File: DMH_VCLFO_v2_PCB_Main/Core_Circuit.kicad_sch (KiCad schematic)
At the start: 21 parts, among them Q5 BS170, U10 TL074, U11 TL074

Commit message: Designed osc core based on slew module
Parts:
- removed C7: 10nF, Capacitor_THT:C_Disc_D4.3mm_W1.9mm_P5.00mm, symbol Device:C
- removed Q5: BS170, Package_TO_SOT_THT:TO-92_Inline, symbol Transistor_FET:BS170
- removed R48, R49: 51k, Resistor_THT:R_Axial_DIN0207_L6.3mm_D2.5mm_P7.62mm_Horizontal, symbol Device:R_US
- removed U10, U11: TL074, Package_DIP:DIP-14_W7.62mm_Socket, symbol Amplifier_Operational:TL074
- added C13, C14, C15: 100nF, Capacitor_THT:C_Disc_D4.3mm_W1.9mm_P5.00mm, symbol Device:C
- added C14: 22nF, Capacitor_THT:C_Disc_D4.3mm_W1.9mm_P5.00mm, symbol Device:C
- added C15: 220nF, Capacitor_THT:C_Disc_D4.3mm_W1.9mm_P5.00mm, symbol Device:C
- added C7: 2.2nF, Capacitor_THT:C_Disc_D4.3mm_W1.9mm_P5.00mm, symbol Device:C
- added C7: 10pF, Capacitor_THT:C_Disc_D3.0mm_W2.0mm_P2.50mm, symbol Device:C
- added J12: Conn_02x06_Top_Bottom, Connector_PinHeader_2.54mm:PinHeader_2x06_P2.54mm_Horizontal, symbol Connector_Generic:Conn_02x06_Top_Bottom
- added J13 (x2): Conn_02x03_Top_Bottom, Connector_PinHeader_2.54mm:PinHeader_2x03_P2.54mm_Horizontal, symbol Connector_Generic:Conn_02x03_Top_Bottom
- added J14, J16: Conn_02x03_Top_Bottom, Connector_PinSocket_2.54mm:PinSocket_2x03_P2.54mm_Vertical, symbol Connector_Generic:Conn_02x03_Top_Bottom
- added J15: Conn_02x06_Top_Bottom, Connector_PinSocket_2.54mm:PinSocket_2x06_P2.54mm_Vertical, symbol Connector_Generic:Conn_02x06_Top_Bottom
- added Q10, Q9: BC558, Package_TO_SOT_THT:TO-92L_Inline_Wide, symbol Transistor_BJT:BC558
- added Q5, Q8: BC548, Package_TO_SOT_THT:TO-92L_Inline_Wide, symbol Transistor_BJT:BC548
- added R87, R99: 100k, Resistor_THT:R_Axial_DIN0207_L6.3mm_D2.5mm_P7.62mm_Horizontal, symbol Device:R_US
- added R88: 220k, Resistor_THT:R_Axial_DIN0207_L6.3mm_D2.5mm_P7.62mm_Horizontal, symbol Device:R_US
- added R93: 1k, Resistor_THT:R_Axial_DIN0207_L6.3mm_D2.5mm_P7.62mm_Horizontal, symbol Device:R_US
- added U5, U6: TL074, Package_DIP:DIP-14_W7.62mm_Socket, symbol Amplifier_Operational:TL074
- C6: value 1uF -> 10pF; footprint Capacitor_THT:C_Disc_D4.3mm_W1.9mm_P5.00mm -> Capacitor_THT:C_Disc_D3.0mm_W2.0mm_P2.50mm
- R40: value 100k -> 1k; now not fitted
- R45: value 100k -> 82k
- R46: value 51k -> 100k
- R52: value 3k9 -> 220k
- R56: value 10k -> 100k
- R59: value 10k -> 1k8
- R72, R73: value 100k -> 1k8
- R84: value 680k -> 1k8
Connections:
- net Pot In is gone; now on an unnamed net: R38.1
- net Rng_Sw_2 is gone; now on an unnamed net: R45.2
- net GND: now also C12.2, R43.2, R59.1, R72.1, R73.2, C13.1, C14.2, C15.1, J12.5 (Pin_5), J12.6 (Pin_6), J13.5 (Pin_5), J13.6 (Pin_6), J14.5 (Pin_5), J14.6 (Pin_6), J15.5 (Pin_5), J15.6 (Pin_6), U5.3 (+), U6.12 (+), U6.5 (+); no longer R40.1, R52.2, R56.2, R73.1
- net at R53.1: now also Q10.3 (E), Q5.3 (E), Q8.3 (E), Q9.3 (E); no longer R52.1
- net at R56.1: now also R38.2, R87.1, U5.1; no longer R59.1
- net at R43.1: now also U6.10 (+); no longer R40.2
- net A_Sqr_S: now reaches R46.2
- net A_Sqr_S: now also R45.1, C7.2, J13.3 (Pin_3), U6.8
- net at R72.2: now also Q8.2 (B); no longer R73.2
- net CV In: no longer names the net of R37.1
- net CV In: now also R99.1, U5.2 (-)
- net Rng_Sw_1: no longer names the net of C6.1
- net Rng_Sw_1: now also R46.1, Q10.1 (C), Q5.1 (C), U6.13 (-)
- net Rng_Sw_3 renamed +12V
- net +12V: now also R52.1, C14.1, J13.1 (Pin_1), J14.1 (Pin_1), R88.1, U5.4 (V+), U6.4 (V+)
- removed net Sqr_Raw: R53.2, R59.2, R72.1
- net Tri_Raw: no longer names the net of C6.2
- net Tri_Raw: now also R53.2, U6.14; no longer C12.2
- new net: Q10.2 (B), R84.1
- new net: C7.1, R40.1, U6.9 (-)
- new net: C14.1, C15.1, C7.1, Q8.1 (C), Q9.1 (C), U6.6 (-)
- new net: Q5.2 (B), R52.2, R56.2, R59.2
- new net: Q9.2 (B), R73.1, R87.2, R88.2
- new net: R93.2, U6.7
- new net -12V: C13.2, C15.2, J13.3 (Pin_3), J13.4 (Pin_4), J14.3 (Pin_3), J14.4 (Pin_4), U5.11 (V-), U6.11 (V-)
- new net A_CV_M: J16.5 (Pin_5)
- new net A_CV_S: J13.5 (Pin_5), R37.2
- new net A_Freq_Pot_p2_M: R99.2
- new net A_Rng_Sw_p1_M: J15.12 (Pin_12)
- new net A_Rng_Sw_p1_S: C14.2, J12.12 (Pin_12)
- new net A_Rng_Sw_p3_M: J15.11 (Pin_11)
- new net A_Rng_Sw_p3_S: C15.2, J12.11 (Pin_11)
- new net A_Sqr_M: J16.3 (Pin_3)
- new net A_Tri_M: J16.6 (Pin_6)
- new net A_Tri_S: C7.2, J13.6 (Pin_6), R40.2, R93.1
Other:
- note added: "22pF in bb"
- note added: "Check if this 1k can be removed"
- note added: "Check if this is really the square output"

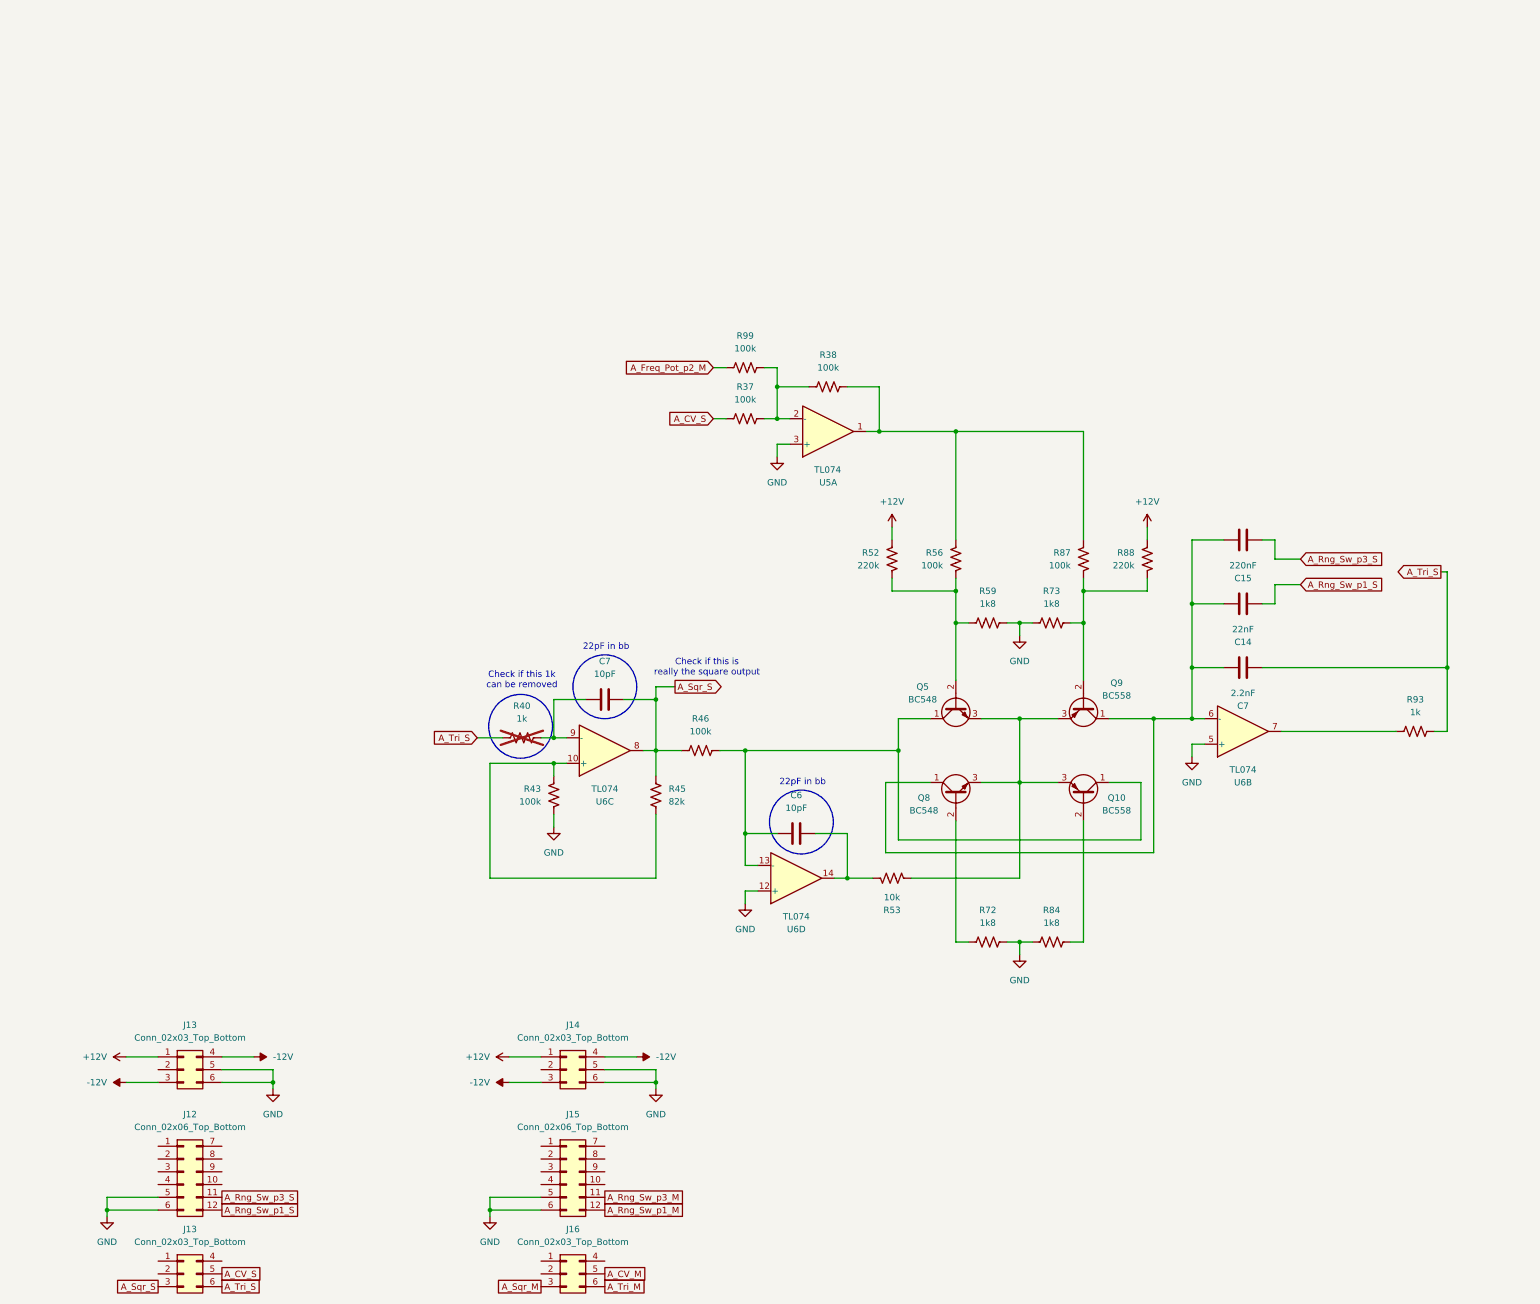
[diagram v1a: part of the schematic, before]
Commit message: Adapted sync reset circuit
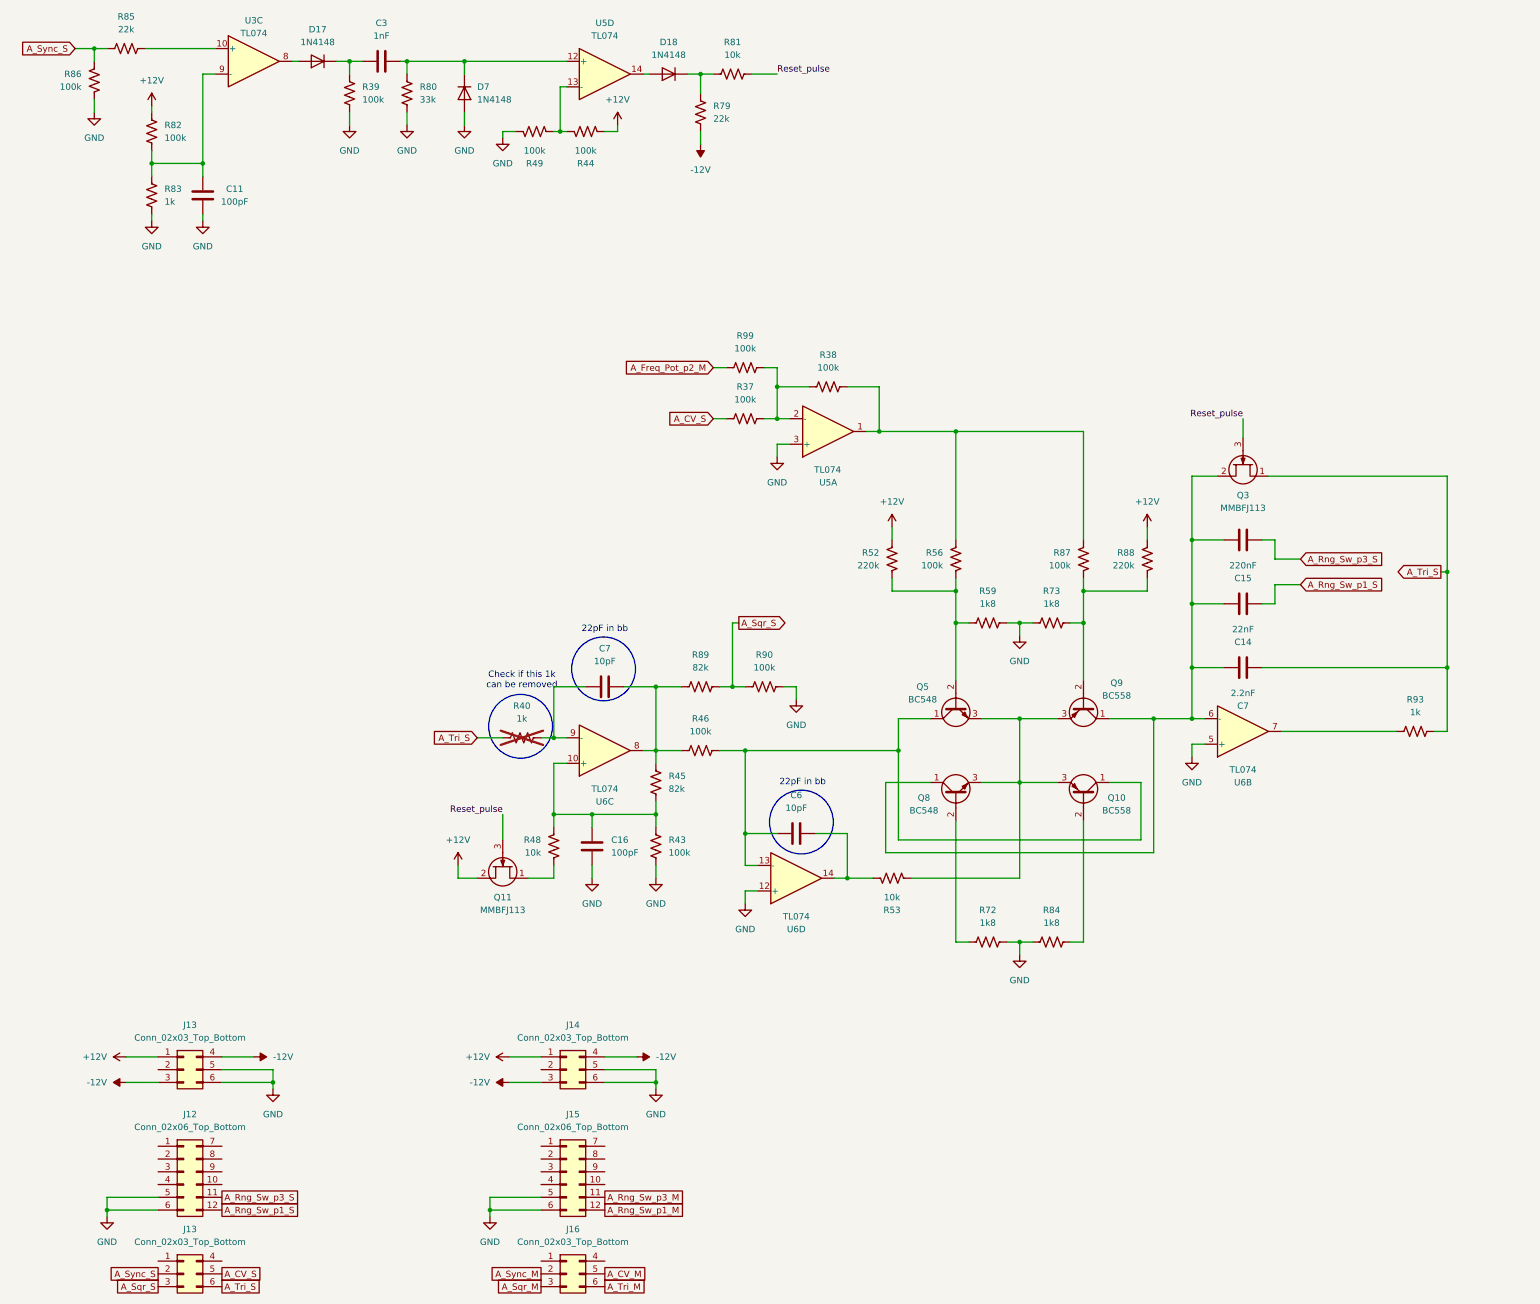
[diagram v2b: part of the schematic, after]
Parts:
- added C11: 100pF, Capacitor_THT:C_Disc_D4.3mm_W1.9mm_P5.00mm, symbol Device:C
- added C16: 100pF, Capacitor_THT:C_Disc_D3.0mm_W2.0mm_P2.50mm, symbol Device:C
- added C3: 1nF, Capacitor_THT:C_Disc_D4.3mm_W1.9mm_P5.00mm, symbol Device:C
- added D17, D18, D7: 1N4148, Diode_THT:D_DO-35_SOD27_P7.62mm_Horizontal, symbol Diode:1N4148
- added Q11, Q3: MMBFJ113, Package_TO_SOT_SMD:SOT-23, symbol Transistor_FET:MMBFJ113
- added R39, R44, R49, R82, R86, R90: 100k, Resistor_THT:R_Axial_DIN0207_L6.3mm_D2.5mm_P7.62mm_Horizontal, symbol Device:R_US
- added R48, R81: 10k, Resistor_THT:R_Axial_DIN0207_L6.3mm_D2.5mm_P7.62mm_Horizontal, symbol Device:R_US
- added R79, R85: 22k, Resistor_THT:R_Axial_DIN0207_L6.3mm_D2.5mm_P7.62mm_Horizontal, symbol Device:R_US
- added R80: 33k, Resistor_THT:R_Axial_DIN0207_L6.3mm_D2.5mm_P7.62mm_Horizontal, symbol Device:R_US
- added R83: 1k, Resistor_THT:R_Axial_DIN0207_L6.3mm_D2.5mm_P7.62mm_Horizontal, symbol Device:R_US
- added R89: 82k, Resistor_THT:R_Axial_DIN0207_L6.3mm_D2.5mm_P7.62mm_Horizontal, symbol Device:R_US
- added U3: TL074, Package_DIP:DIP-14_W7.62mm_Socket, symbol Amplifier_Operational:TL074
- added unit 4 of U5
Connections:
- net +12V: now also Q11.2 (S), R44.1, R82.1
- net -12V: now also R79.2
- net A_Sqr_S: now also R89.1, R90.2; no longer C7.2, R45.1, R46.2, U6.8
- net A_Tri_S: now also Q3.1 (D)
- net GND: now also C11.1, C16.1, D7.2 (A), R39.2, R49.2, R80.2, R83.2, R86.1, R90.1
- net at R43.1, R45.2, U6.10 (+): now also C16.2, R48.1
- net at C14.1, C15.1, C7.1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: now also Q3.2 (S)
- net A_Sync_M: now reaches J16.2 (Pin_2)
- net A_Sync_S: now reaches J13.2 (Pin_2)
- net A_Sync_S: now also R85.1, R86.2
- new net: C3.1, D17.1 (K), R39.1
- new net: C7.2, R45.1, R46.2, R89.2, U6.8
- new net: R85.2, U3.10 (+)
- new net: C11.2, R82.2, R83.1, U3.9 (-)
- new net: R44.2, R49.1, U5.13 (-)
- new net: Q11.1 (D), R48.2
- new net: D18.1 (K), R79.1, R81.2
- new net: C3.2, D7.1 (K), R80.1, U5.12 (+)
- new net: D17.2 (A), U3.8
- new net: D18.2 (A), U5.14
- new net Reset_pulse: Q11.3 (G), Q3.3 (G), R81.1
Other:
- note removed: "Check if this is really the square output"
- moved on the sheet: C7, R43, R45

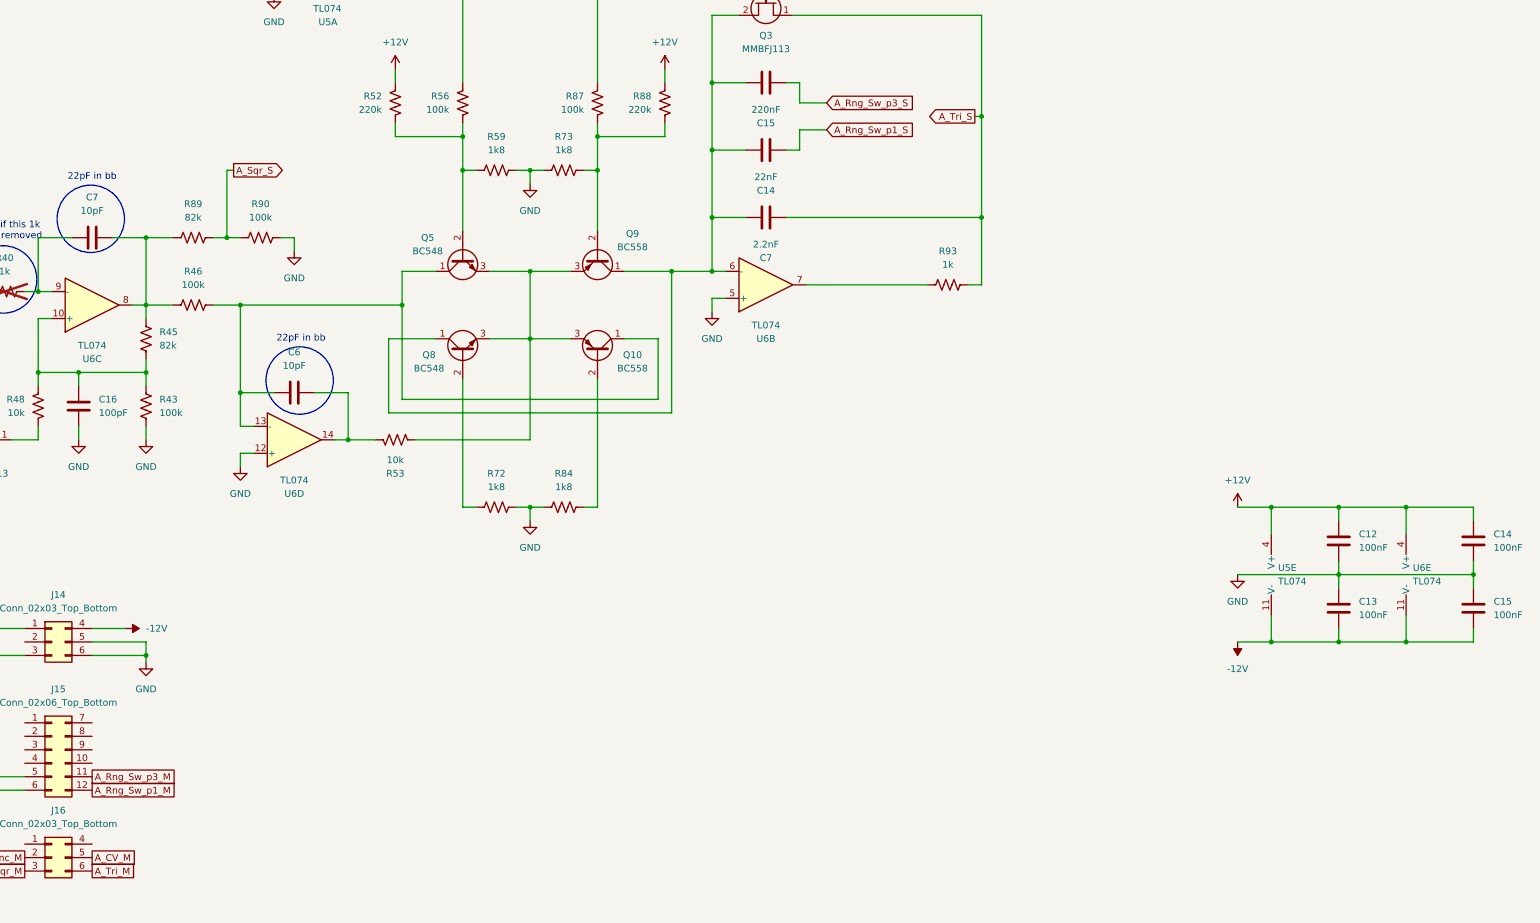
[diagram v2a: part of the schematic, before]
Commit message: Adapted saw shaper
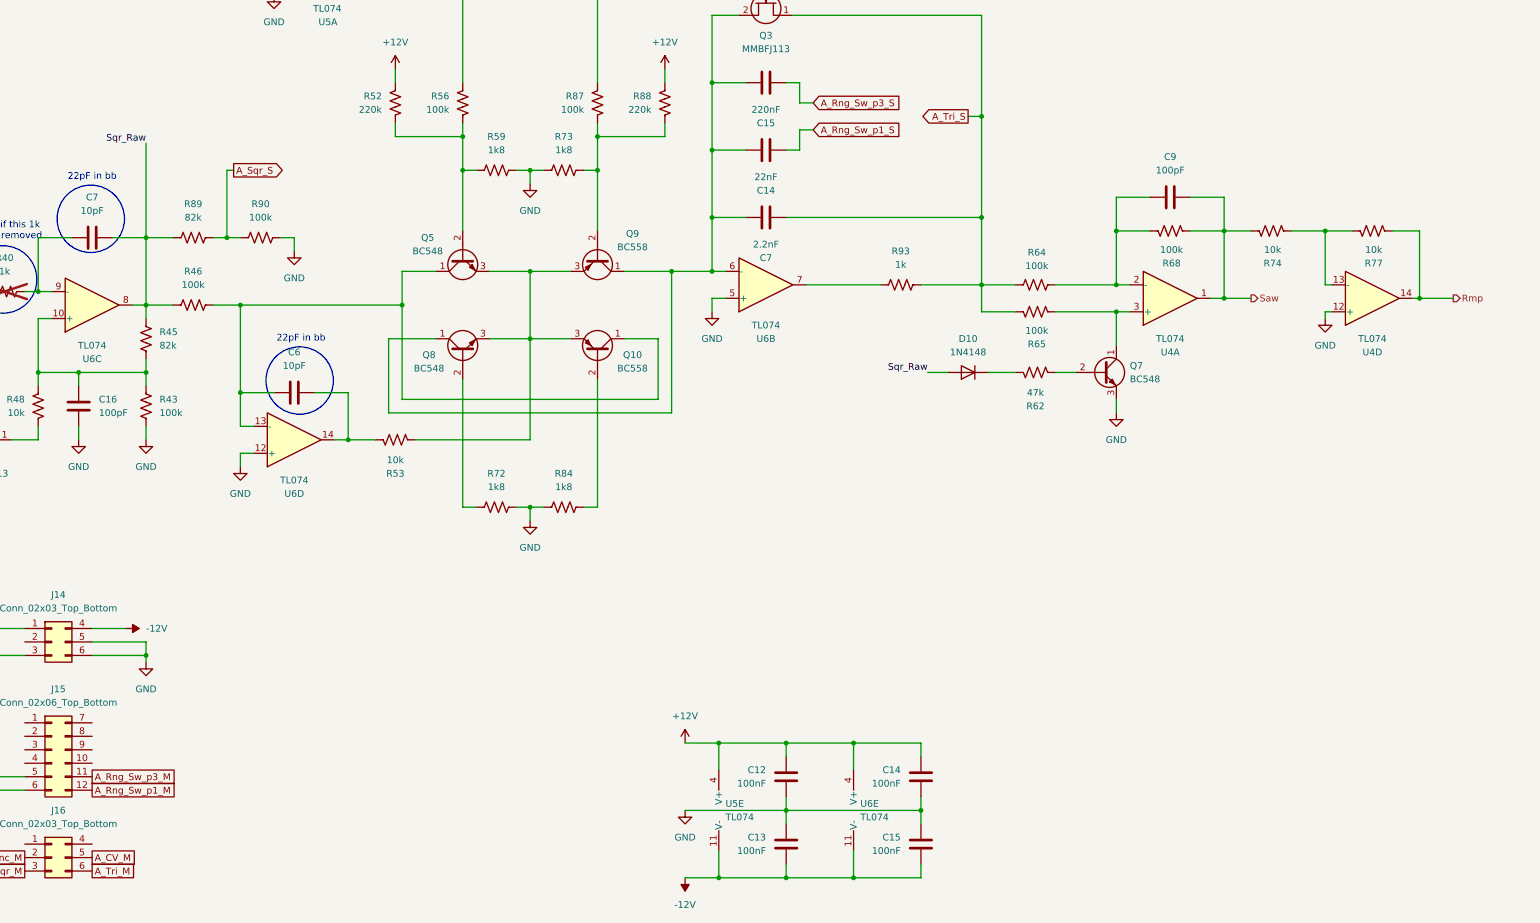
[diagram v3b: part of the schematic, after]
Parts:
- added C9: 100pF, Capacitor_THT:C_Disc_D4.3mm_W1.9mm_P5.00mm, symbol Device:C
- added D10: 1N4148, Diode_THT:D_DO-35_SOD27_P7.62mm_Horizontal, symbol Diode:1N4148
- added Q7: BC548, Package_TO_SOT_THT:TO-92L_Inline_Wide, symbol Transistor_BJT:BC548
- added R62: 47k, Resistor_THT:R_Axial_DIN0207_L6.3mm_D2.5mm_P7.62mm_Horizontal, symbol Device:R_US
- added R64, R65, R68: 100k, Resistor_THT:R_Axial_DIN0207_L6.3mm_D2.5mm_P7.62mm_Horizontal, symbol Device:R_US
- added R74, R77: 10k, Resistor_THT:R_Axial_DIN0207_L6.3mm_D2.5mm_P7.62mm_Horizontal, symbol Device:R_US
- added U4: TL074, Package_DIP:DIP-14_W7.62mm_Socket, symbol Amplifier_Operational:TL074
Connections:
- net A_Tri_S: now also R64.1, R65.1
- net GND: now also Q7.3 (E), U4.12 (+)
- net Sqr_Raw: now reaches C7.2, R45.1, R46.2, R89.2, U6.8
- net Sqr_Raw: now also D10.2 (A)
- new net: C9.1, R64.2, R68.1, U4.2 (-)
- new net: Q7.1 (C), R65.2, U4.3 (+)
- new net: R74.2, R77.1, U4.13 (-)
- new net: D10.1 (K), R62.1
- new net: Q7.2 (B), R62.2
- new net Rmp: R77.2, U4.14
- new net Saw: C9.2, R68.2, R74.1, U4.1
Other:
- moved on the sheet: C12, C13, C14, C15, R93, U5E, U6E
